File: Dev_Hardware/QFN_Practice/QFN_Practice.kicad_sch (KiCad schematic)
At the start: 8 parts, among them J1 USB_C_Receptacle_USB2.0_16P, SW1 SW_Push, SW2 SW_Push, U1 LPC824M201JHI33, U2 CP2102N-Axx-xQFN20

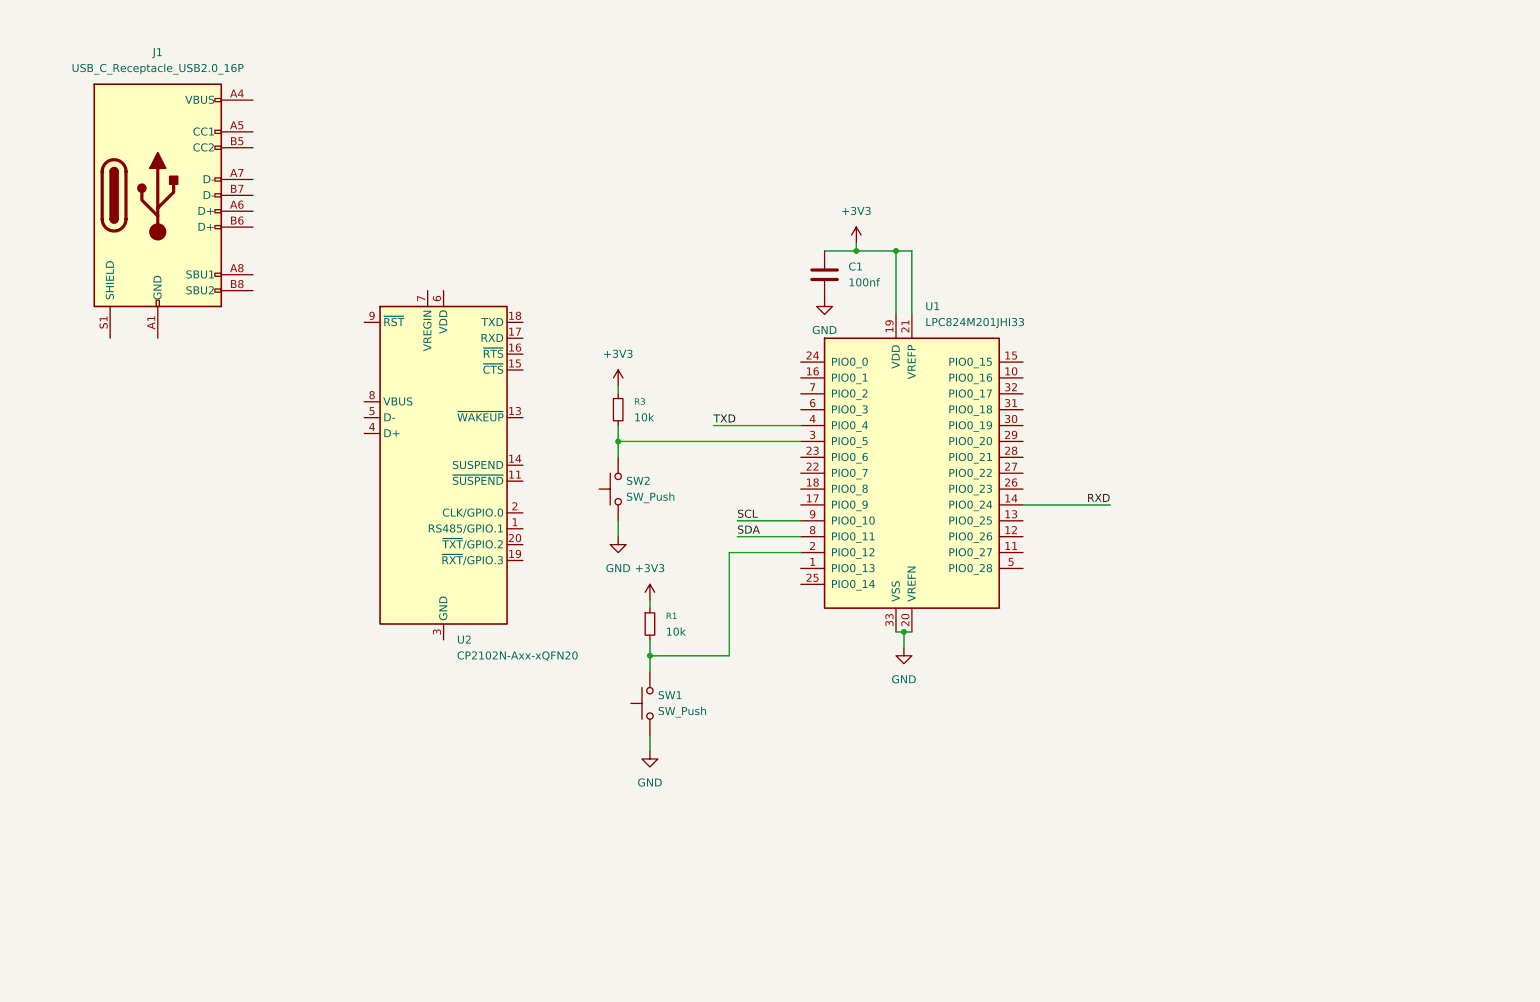
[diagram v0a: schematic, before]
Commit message: Added USB wiring and power wiring
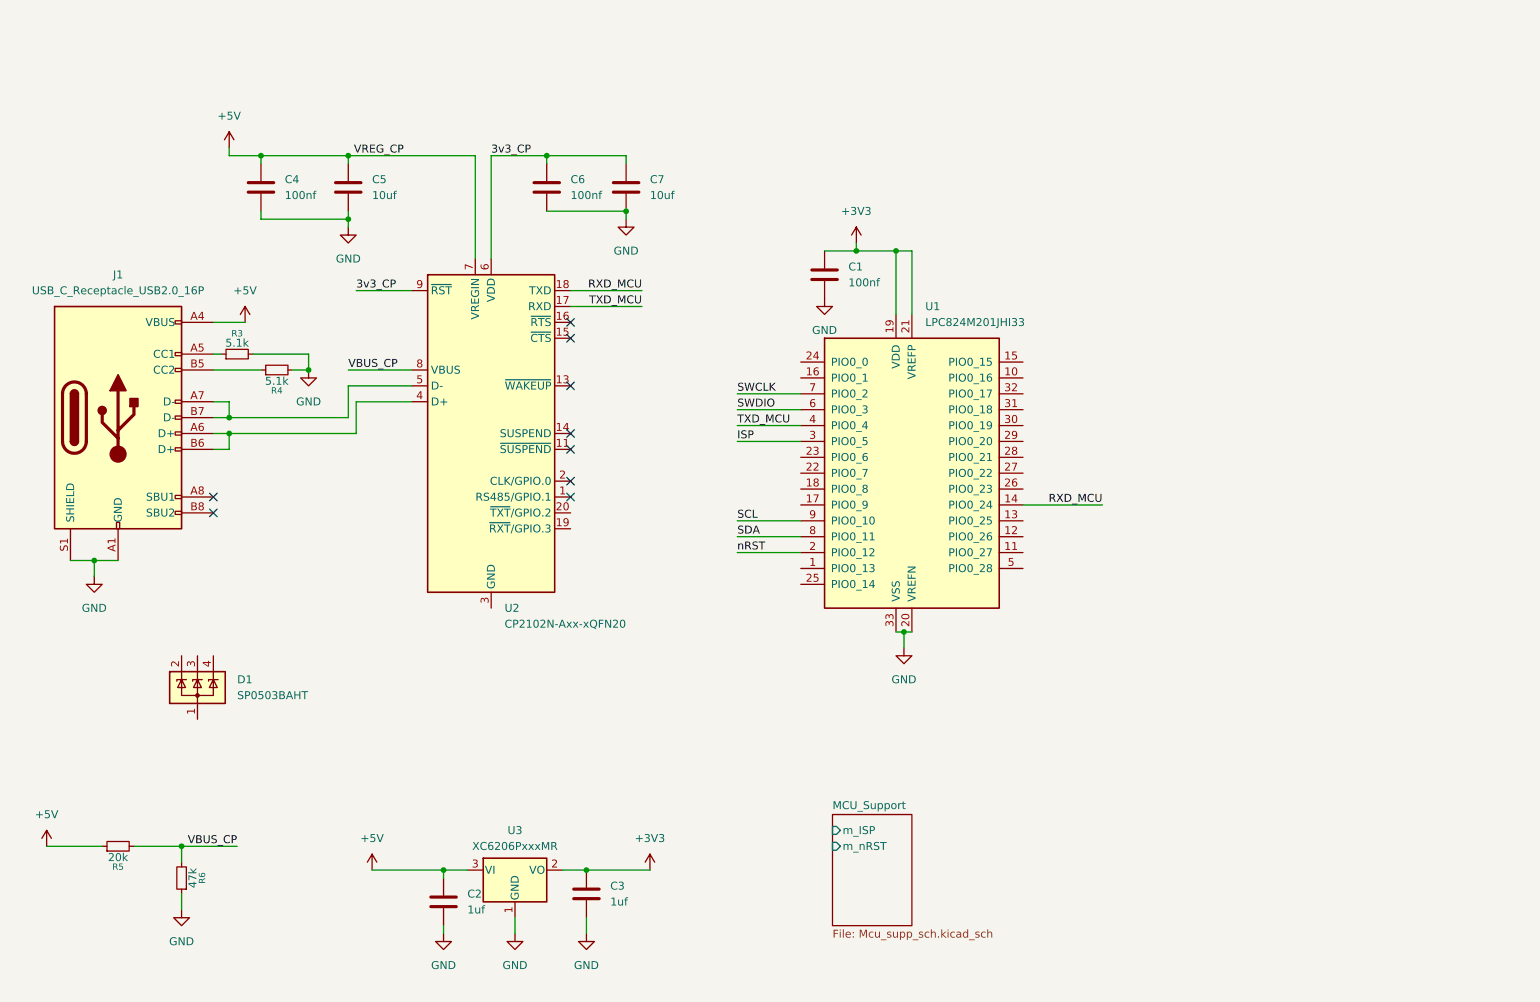
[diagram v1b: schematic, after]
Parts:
- removed R1: 10k, Resistor_SMD:R_0603_1608Metric, symbol Device:R_Small
- removed SW1, SW2: SW_Push, Button_Switch_SMD:SW_SPST_TS-1088-xR020, symbol Switch:SW_Push
- added C2, C3: 1uf, Capacitor_SMD:C_0603_1608Metric, symbol Device:C
- added C4, C6: 100nf, Capacitor_SMD:C_0603_1608Metric, symbol Device:C
- added C5, C7: 10uf, Capacitor_SMD:C_0603_1608Metric, symbol Device:C
- added D1: SP0503BAHT, Package_TO_SOT_SMD:SOT-143, symbol Power_Protection:SP0503BAHT
- added R4: 5.1k, Resistor_SMD:R_0603_1608Metric, symbol Device:R_Small
- added R5: 20k, Resistor_SMD:R_0603_1608Metric, symbol Device:R_Small
- added R6: 47k, Resistor_SMD:R_0603_1608Metric, symbol Device:R_Small
- added U3: XC6206PxxxMR, Package_TO_SOT_SMD:SOT-23-3, symbol Regulator_Linear:XC6206PxxxMR
- R3: value 10k -> 5.1k
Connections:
- net RXD is gone; now on net RXD_MCU: U1.14 (PIO0_24)
- net TXD is gone; now on net TXD_MCU: U1.4 (PIO0_4)
- net +3V3: now also C3.1, U3.2 (VO); no longer R3.1
- net GND: now also J1.A1 (GND), J1.A12 (GND), J1.B1 (GND), J1.B12 (GND), J1.S1 (SHIELD), R3.2, C2.2, C3.2, C4.2, C5.2, C6.2, C7.2, R4.2, R6.1, U3.1 (GND)
- net ISP: now reaches U1.3 (PIO0_5)
- net ISP: no longer R3.2
- net +5V: now reaches J1.A4 (VBUS), J1.A9 (VBUS), J1.B4 (VBUS), J1.B9 (VBUS)
- net +5V: now also U2.7 (VREGIN), C2.1, C4.1, C5.1, R5.1, U3.3 (VI)
- net at J1.A5 (CC1): now also R3.1
- net at J1.A6 (D+): now also J1.B6 (D+), U2.4 (D+)
- net at J1.A7 (D-): now also J1.B7 (D-), U2.5 (D-)
- net at J1.B5 (CC2): now also R4.1
- net nRST: now reaches U1.2 (PIO0_12)
- net SWDIO: now reaches U1.6 (PIO0_3)
- net SWCLK: now reaches U1.7 (PIO0_2)
- net TXD_MCU: now reaches U2.17 (RXD)
- net RXD_MCU: now reaches U2.18 (TXD)
- net 3v3_CP: now reaches U2.6 (VDD)
- net 3v3_CP: now also U2.9 (~{RST}), C6.1, C7.1
- net VBUS_CP: now reaches U2.8 (VBUS)
- net VBUS_CP: now also R5.2, R6.2
- no-connect marks 0 -> 9
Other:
- added sheet MCU_Support (Mcu_supp_sch.kicad_sch)
- moved on the sheet: J1, U2

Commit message: Finish schematics for QFN board, started routing USB
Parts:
- removed D1: SP0503BAHT, Package_TO_SOT_SMD:SOT-143, symbol Power_Protection:SP0503BAHT
- added D2: NCD0805R1, LED_SMD:LED_0805_2012Metric, symbol Device:LED
- added D3, D4: KT0805-G, LED_SMD:LED_0805_2012Metric, symbol Device:LED
- added J3, J4: Conn_01x14_Pin, Connector_PinHeader_2.54mm:PinHeader_1x14_P2.54mm_Vertical, symbol Connector:Conn_01x14_Pin
- added JP1, JP2: lumper, Jumper:SolderJumper-2_P1.3mm_Open_RoundedPad1.0x1.5mm, symbol Jumper:SolderJumper_2_Open
- added R10, R11: 4.7k, Resistor_SMD:R_0603_1608Metric, symbol Device:R_Small
- added R7, R8, R9: 20k, Resistor_SMD:R_0603_1608Metric, symbol Device:R_Small
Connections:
- net +3V3: now also JP1.2 (B), JP2.2 (B)
- net +5V: now also J4.12 (Pin_12)
- net 3v3_CP: now also R7.1, R8.1
- net GND: now also U2.12 (GND), U2.21 (GND), U2.3 (GND), J4.13 (Pin_13), J4.14 (Pin_14), R9.2
- net RXD_MCU: now also J4.11 (Pin_11)
- net SCL: now also J4.7 (Pin_7)
- net SDA: now also J4.8 (Pin_8), R10.2, R11.2
- net TXD_MCU: now also J4.10 (Pin_10)
- net D+: now reaches J1.A6 (D+), J1.B6 (D+), U2.4 (D+)
- net D-: now reaches J1.A7 (D-), J1.B7 (D-), U2.5 (D-)
- net at U1.1 (PIO0_13): now also D4.2 (A)
- net at U1.10 (PIO0_16): now also J3.2 (Pin_2)
- net at U1.11 (PIO0_27): now also J3.13 (Pin_13)
- net at U1.12 (PIO0_26): now also J3.12 (Pin_12)
- net at U1.13 (PIO0_25): now also J3.11 (Pin_11)
- net at U1.15 (PIO0_15): now also J3.1 (Pin_1)
- net P2: now reaches U1.16 (PIO0_1)
- net P2: now also J4.2 (Pin_2)
- net P9: now reaches U1.17 (PIO0_9)
- net P9: now also J4.6 (Pin_6)
- net P8: now reaches U1.18 (PIO0_8)
- net P8: now also J4.5 (Pin_5)
- net P7: now reaches U1.22 (PIO0_7)
- net P7: now also J4.4 (Pin_4)
- net P6: now reaches U1.23 (PIO0_6)
- net P6: now also J4.3 (Pin_3)
- net P1: now reaches U1.24 (PIO0_0)
- net P1: now also J4.1 (Pin_1)
- net P14: now reaches U1.25 (PIO0_14)
- net P14: now also J4.9 (Pin_9)
- net at U1.26 (PIO0_23): now also J3.9 (Pin_9)
- net at U1.27 (PIO0_22): now also J3.8 (Pin_8)
- net at U1.28 (PIO0_21): now also J3.7 (Pin_7)
- net at U1.29 (PIO0_20): now also J3.6 (Pin_6)
- net at U1.30 (PIO0_19): now also J3.5 (Pin_5)
- net at U1.31 (PIO0_18): now also J3.4 (Pin_4)
- net at U1.32 (PIO0_17): now also J3.3 (Pin_3)
- net at U1.5 (PIO0_28): now also J3.14 (Pin_14)
- net at U2.19 (~{RXT}/GPIO.3): now also D2.1 (K)
- net at U2.20 (~{TXT}/GPIO.2): now also D3.1 (K)
- new net: JP2.1 (A), R11.1
- new net: D2.2 (A), R8.2
- new net: JP1.1 (A), R10.1
- new net: D4.1 (K), R9.1
- new net: D3.2 (A), R7.2

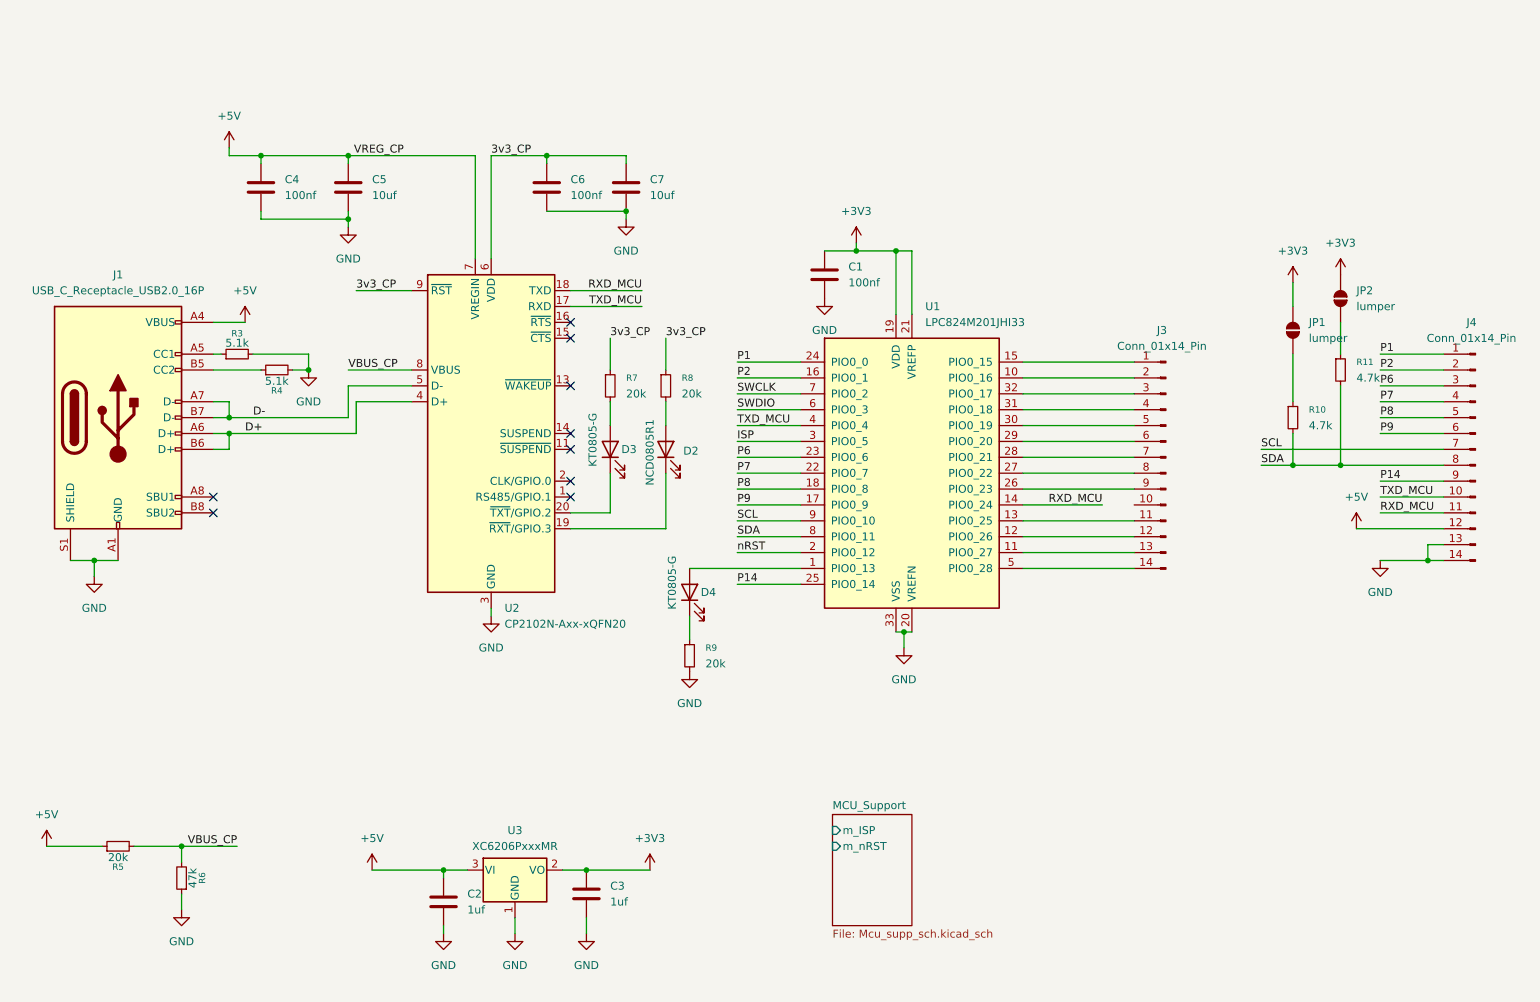
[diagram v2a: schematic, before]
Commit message: finished routing for all but power regulation and GPIO
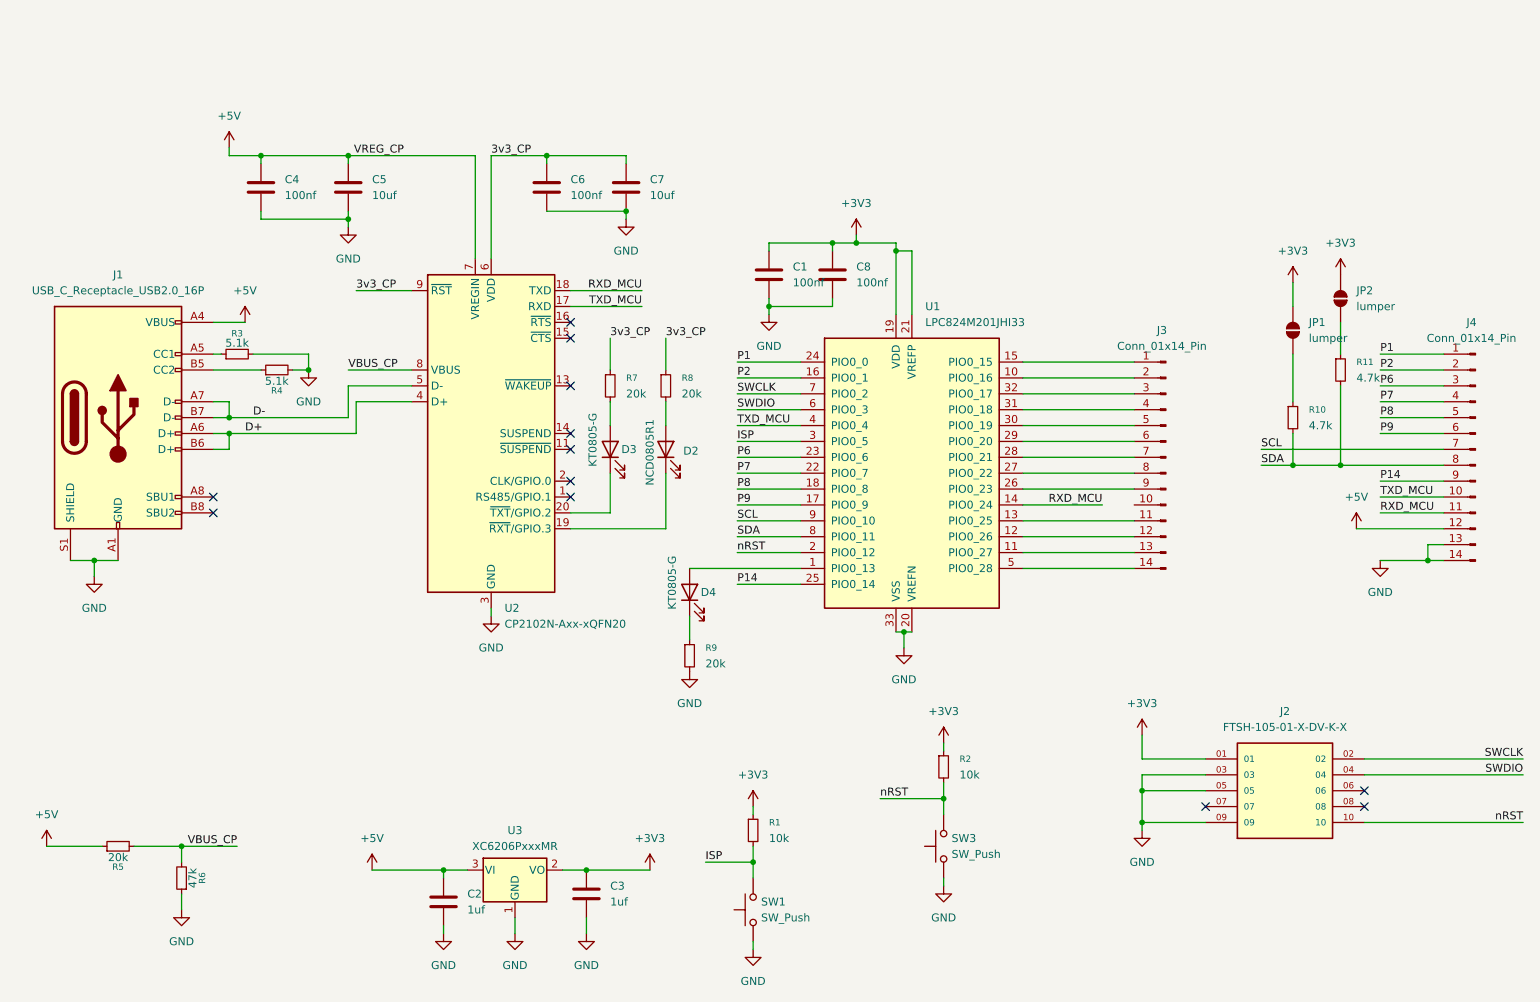
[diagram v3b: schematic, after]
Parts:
- added C8: 100nf, Capacitor_SMD:C_0603_1608Metric, symbol Device:C
- added J2: FTSH-105-01-X-DV-K-X, FTSH_105_01_L_DV_K:SAMTEC_FTSH-105-01-X-DV-K-X, symbol FTSH-105-01-X-DV-K-X:FTSH-105-01-X-DV-K-X
- added R1, R2: 10k, Resistor_SMD:R_0603_1608Metric, symbol Device:R_Small
- added SW1, SW3: SW_Push, Button_Switch_SMD:SW_SPST_TS-1088-xR020, symbol Switch:SW_Push
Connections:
- net +3V3: now also C8.1, J2.01, R1.1, R2.1
- net GND: now also C8.2, J2.03, J2.05, J2.09, SW1.1, SW3.1
- net ISP: now also R1.2, SW1.2
- net SWCLK: now also J2.02
- net SWDIO: now also J2.04
- net nRST: now also J2.10, R2.2, SW3.2
- no-connect marks 9 -> 12
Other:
- removed sheet MCU_Support
- moved on the sheet: C1

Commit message: finished layout
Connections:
- net SCL: now also R11.2
- net SDA: no longer R11.2
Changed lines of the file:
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@@
-	)
-	(junction
-		(at 231.14 93.98)
-		(diameter 0)
-		(color 0 0 0 0)
 	)
 	(junction
@@
 		(color 0 0 0 0)
 	)
+	(junction
+		(at 231.14 91.44)
+		(diameter 0)
+		(color 0 0 0 0)
+	)
 	(no_connect
 		(at 107.95 99.06)
@@
 	(wire
 		(pts
-			(xy 231.14 81.28) (xy 231.14 93.98)
-		)
-		(stroke
-			(width 0)
-			(type default)
-		)
-	)
-	(wire
-		(pts
 			(xy 134.62 102.87) (xy 144.78 102.87)
 		)
@@
 	(wire
 		(pts
-			(xy 218.44 91.44) (xy 247.65 91.44)
+			(xy 218.44 91.44) (xy 231.14 91.44)
 		)
 		(stroke
@@
 	(wire
 		(pts
+			(xy 231.14 91.44) (xy 247.65 91.44)
+		)
+		(stroke
+			(width 0)
+			(type default)
+		)
+	)
+	(wire
+		(pts
 			(xy 53.34 43.18) (xy 53.34 44.45)
 		)
@@
 	(wire
 		(pts
-			(xy 223.52 93.98) (xy 231.14 93.98)
+			(xy 231.14 81.28) (xy 231.14 91.44)
 		)
 		(stroke
@@
 	(wire
 		(pts
-			(xy 231.14 93.98) (xy 247.65 93.98)
-		)
-		(stroke
+			(xy 223.52 93.98) (xy 247.65 93.98)
+		)
+		(stroke

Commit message: finished layout and routing
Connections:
- net +5V: now also J4.1 (Pin_1); no longer J4.12 (Pin_12)
- net GND: now also J4.2 (Pin_2), J4.3 (Pin_3); no longer J4.13 (Pin_13), J4.14 (Pin_14)
- net P1: now also J3.7 (Pin_7); no longer J4.1 (Pin_1)
- net P14: now also J3.8 (Pin_8); no longer J4.9 (Pin_9)
- net P2: now also J4.4 (Pin_4); no longer J4.2 (Pin_2)
- net P6: now also J3.6 (Pin_6); no longer J4.3 (Pin_3)
- net P7: now also J3.5 (Pin_5); no longer J4.4 (Pin_4)
- net P8: now also J3.4 (Pin_4); no longer J4.5 (Pin_5)
- net P9: now also J3.3 (Pin_3); no longer J4.6 (Pin_6)
- net P15: now reaches J3.1 (Pin_1), U1.15 (PIO0_15)
- net P22: now reaches J3.10 (Pin_10)
- net P22: now also U1.27 (PIO0_22)
- net P25: now reaches J3.11 (Pin_11), U1.13 (PIO0_25)
- net P26: now reaches J3.12 (Pin_12), U1.12 (PIO0_26)
- net P27: now reaches J3.13 (Pin_13), U1.11 (PIO0_27)
- net P28: now reaches J3.14 (Pin_14), U1.5 (PIO0_28)
- net P16: now reaches J3.2 (Pin_2), U1.10 (PIO0_16)
- net P17: now reaches U1.32 (PIO0_17)
- net P17: now also J4.6 (Pin_6); no longer J3.3 (Pin_3)
- net P18: now reaches U1.31 (PIO0_18)
- net P18: now also J4.9 (Pin_9); no longer J3.4 (Pin_4)
- net P19: now reaches U1.30 (PIO0_19)
- net P19: now also J4.12 (Pin_12); no longer J3.5 (Pin_5)
- net P20: now reaches U1.29 (PIO0_20)
- net P20: now also J4.13 (Pin_13); no longer J3.6 (Pin_6)
- net P21: now reaches U1.28 (PIO0_21)
- net P21: now also J4.14 (Pin_14); no longer J3.7 (Pin_7)
- net P23: now reaches J3.9 (Pin_9), U1.26 (PIO0_23)
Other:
- moved on the sheet: J3, JP1, JP2, R10, R11
